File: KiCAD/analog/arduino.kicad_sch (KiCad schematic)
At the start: 50 parts, among them J11 Screw_Terminal_01x03, J12 Screw_Terminal_01x04, J13 Screw_Terminal_01x03, J14 Screw_Terminal_01x05, J16 Screw_Terminal_01x03, J17 Conn_Coaxial_Small, J18 Conn_Coaxial_Small, J19 Conn_Coaxial_Small, J20 Screw_Terminal_01x04, J21 Screw_Terminal_01x02, J22 Screw_Terminal_01x04, J23 Conn_Coaxial_Small, J24 Conn_Coaxial_Small, J6 Screw_Terminal_01x02, J7 Screw_Terminal_01x02, J8 Screw_Terminal_01x02, Q4 2N7000, Q5 2N7000, Q6 2N7000, Q7 2N7000, U1 MCP1700x-330xxTO, U17 Adafruit_PCF8575_Breakout, U18 CD14538B, U3 MCP4728

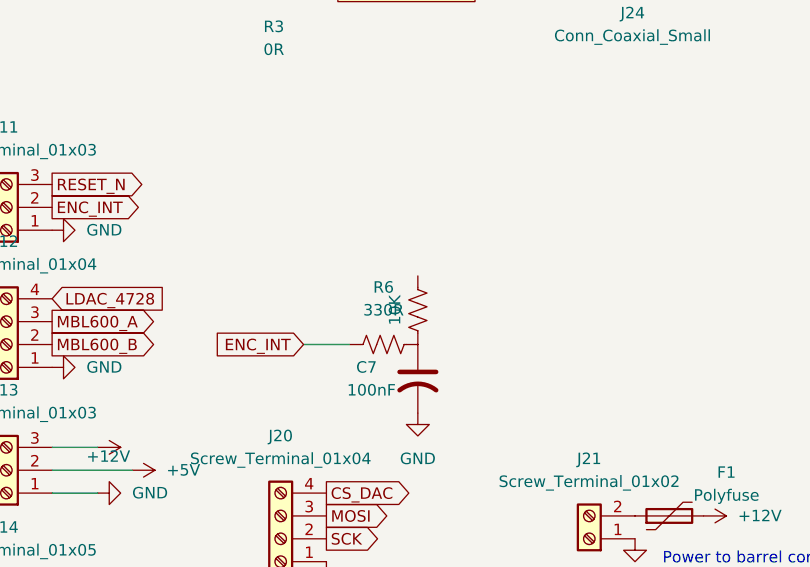
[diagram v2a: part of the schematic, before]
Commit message: KiCad revB: protoshield schematic complete + 1N4728A symbol + misc board edits
Protoshield (Metro ESP32-S3 GPIO signal conditioning):
- Full schematic drawn: series R + bypass C + Zener clamp for I_CATHODE_A/B
  (1k+100nF+1N4728A), MBL600_A/B (10k/20k divider + 22pF), GRID_BLOCK_CRASH
  (1k+100nF), ENC_INT (330R+10k pull-up), PADDLE_A/B (10k pull-ups), RESET_N
  (100nF), TR_SENSE (10k pull-up), passthrough nodes for SPI and LDAC_4728
- All THT footprints assigned (ceramic disc caps, DIN0207 resistors, Phoenix
  MKDS-1.5 2-pin/3-pin terminal blocks)
- ENC_INT wiring gap fixed (R7 re-placed to connect J4 pin 2 to ENC_INT net)
- sym-lib-table added (points to shared xmitter.kicad_sym)
- protoshield.net generated netlist added for reference

Symbol library (xmitter.kicad_sym):
- Added 1N4728A (3.3V 1W Zener, DO-41) with correct KiCad 9.0 inline pts format

Other boards:
- analog/arduino.kicad_sch: minor junction/reference adjustments after Metro
  symbol was removed to protoshield in prior session
- bias: kicad_pro and kicad_sch updated (ongoing schematic work)
- power/sym-lib-table added for new stub project

Added: Purchase Orders (JLCPCB + Digi-Key invoices), tools/_scan_symbols.py

Co-Authored-By: Claude Sonnet 4.6 <noreply@anthropic.com>
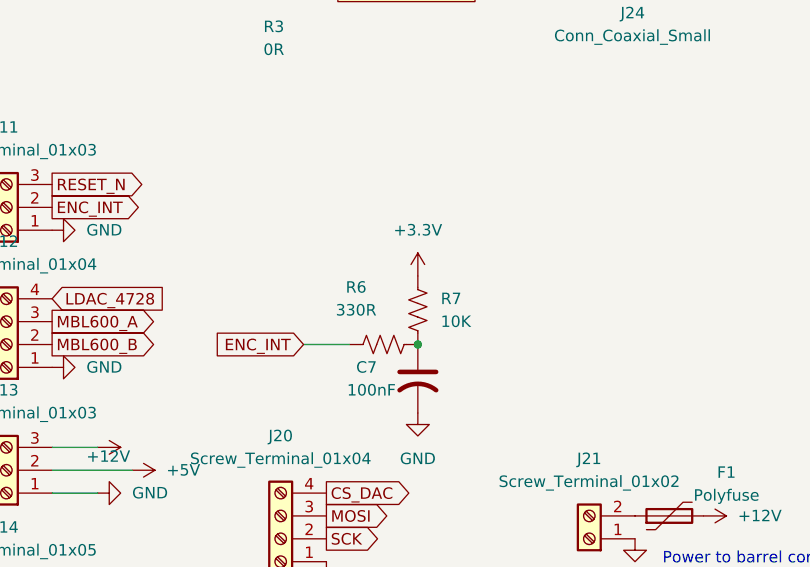
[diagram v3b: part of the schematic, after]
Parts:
- removed R102: 10K, Resistor_THT:R_Axial_DIN0207_L6.3mm_D2.5mm_P10.16mm_Horizontal, symbol Device:R_US
- added R7: 10K, symbol Device:R_US
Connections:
- net +3.3V: now also R7.1
- net at C7.1, R6.2: now also R7.2
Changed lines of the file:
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@@
 	)
 	(junction
+		(at 71.12 81.28)
+		(diameter 0)
+		(color 0 0 0 0)
+	)
+	(junction
 		(at 25.4 36.83)
 		(diameter 0)
@@
 	)
 	(symbol
+		(lib_id "power:+3.3V")
+		(at 71.12 73.66 0)
+		(unit 1)
+		(body_style 1)
+		(exclude_from_sim no)
+		(in_bom yes)
+		(on_board yes)
+		(in_pos_files yes)
+		(dnp no)
+		(fields_autoplaced yes)
+		(property "Reference" "#PWR09"
+			(at 71.12 77.47 0)
+			(hide yes)
+			(show_name no)
+			(do_not_autoplace no)
+			(effects
+				(font
+					(size 1.27 1.27)
+				)
+			)
+		)
+		(property "Value" "+3.3V"
+			(at 71.12 68.58 0)
+			(show_name no)
+			(do_not_autoplace no)
+			(effects
+				(font
+					(size 1.27 1.27)
+				)
+			)
+		)
+		(property "Footprint" ""
+			(at 71.12 73.66 0)
+			(hide yes)
+			(show_name no)
+			(do_not_autoplace no)
+			(effects
+				(font
+					(size 1.27 1.27)
+				)
+			)
+		)
+		(property "Datasheet" ""
+			(at 71.12 73.66 0)
+			(hide yes)
+			(show_name no)
+			(do_not_autoplace no)
+			(effects
+				(font
+					(size 1.27 1.27)
+				)
+			)
+		)
+		(property "Description" "Power symbol creates a global label with name \"+3.3V\""
+			(at 71.12 73.66 0)
+			(hide yes)
+			(show_name no)
+			(do_not_autoplace no)
+			(effects
+				(font
+					(size 1.27 1.27)
+				)
+			)
+		)
+		(pin "1"
+		)
+		(instances
+			(project "analog"
+				(path "/d3de40b8-856b-4fbd-829c-f45ffcd55742/2d83d0b5-86d4-4ced-ab68-6465e3dc2d72"
+					(reference "#PWR09")
+					(unit 1)
+				)
+			)
+		)
+	)
+	(symbol
 		(lib_id "Device:R_US")
 		(at 179.07 149.86 90)
@@
 	)
 	(symbol
+		(lib_id "Device:R_US")
+		(at 71.12 77.47 0)
+		(unit 1)
+		(body_style 1)
+		(exclude_from_sim no)
+		(in_bom yes)
+		(on_board yes)
+		(in_pos_files yes)
+		(dnp no)
+		(fields_autoplaced yes)
+		(property "Reference" "R7"
+			(at 73.66 76.1999 0)
+			(show_name no)
+			(do_not_autoplace no)
+			(effects
+				(font
+					(size 1.27 1.27)
+				)
+				(justify left)
+			)
+		)
+		(property "Value" "10K"
+			(at 73.66 78.7399 0)
+			(show_name no)
+			(do_not_autoplace no)
+			(effects
+				(font
+					(size 1.27 1.27)
+				)
+				(justify left)
+			)
+		)
+		(property "Footprint" ""
+			(at 72.136 77.724 90)
+			(hide yes)
+			(show_name no)
+			(do_not_autoplace no)
+			(effects
+				(font
+					(size 1.27 1.27)
+				)
+			)
+		)
+		(property "Datasheet" ""
+			(at 71.12 77.47 0)
+			(hide yes)
+			(show_name no)
+			(do_not_autoplace no)
+			(effects
+				(font
+					(size 1.27 1.27)
+				)
+			)
+		)
+		(property "Description" "Resistor, US symbol"
+			(at 71.12 77.47 0)
+			(hide yes)
+			(show_name no)
+			(do_not_autoplace no)
+			(effects
+				(font
+					(size 1.27 1.27)
+				)
+			)
+		)
+		(pin "2"
+		)
+		(pin "1"
+		)
+		(instances
+			(project "analog"
+				(path "/d3de40b8-856b-4fbd-829c-f45ffcd55742/2d83d0b5-86d4-4ced-ab68-6465e3dc2d72"
+					(reference "R7")
+					(unit 1)
+				)
+			)
+		)
+	)
+	(symbol
 		(lib_id "Connector:Conn_Coaxial_Small")
 		(at 95.25 36.83 0)
@@
 		(in_pos_files yes)
 		(dnp no)
-		(fields_autoplaced yes)
 		(property "Reference" "R6"
-			(at 67.31 74.93 90)
+			(at 64.262 74.93 90)
 			(show_name no)
 			(do_not_autoplace no)
@@
 		)
 		(property "Value" "330R"
-			(at 67.31 77.47 90)
+			(at 64.262 77.47 90)
 			(show_name no)
 			(do_not_autoplace no)
@@
 					(unit 1)
 				)
-			)
-		)
-	)
-	(symbol
-		(lib_id "Device:R_US")
-		(at 71.12 77.47 0)
-		(unit 1)
-		(body_style 1)
-		(exclude_from_sim no)
-		(in_bom yes)
-		(on_board no)
-		(in_pos_files yes)
-		(dnp no)
-		(fields_autoplaced yes)
-		(property "Reference" "R102"
-			(at 73.66 77.47 90)
-			(hide yes)
-			(show_name no)
-			(do_not_autoplace no)
-			(effects
-				(font
-					(size 1.27 1.27)
-				)
-			)
-		)
-		(property "Value" "10K"
-			(at 68.58 77.47 90)
-			(show_name no)
-			(do_not_autoplace no)
-			(effects
-				(font
-					(size 1.27 1.27)
-				)
-			)
-		)
-		(property "Footprint" "Resistor_THT:R_Axial_DIN0207_L6.3mm_D2.5mm_P10.16mm_Horizontal"
-			(at 71.12 77.47 0)
-			(hide yes)
-			(show_name no)
-			(do_not_autoplace no)
-			(effects
-				(font
-					(size 1.27 1.27)
-				)
-			)
-		)
-		(property "Datasheet" ""
-			(at 71.12 77.47 0)
-			(hide yes)
-			(show_name no)
-			(do_not_autoplace no)
-			(effects
-				(font
-					(size 1.27 1.27)
-				)
-			)
-		)
-		(property "Description" "Pull-up for future front-panel ENC_INT signal at Metro D4"
-			(at 71.12 77.47 0)
-			(hide yes)
-			(show_name no)
-			(do_not_autoplace no)
-			(effects
-				(font
-					(size 1.27 1.27)
-				)
-			)
-		)
-		(pin "1"
-		)
-		(pin "2"
-		)
-		(instances
-			(project "analog"
-				(path "/d3de40b8-856b-4fbd-829c-f45ffcd55742/2d83d0b5-86d4-4ced-ab68-6465e3dc2d72"
-					(reference "R102")
-					(unit 1)
-				)

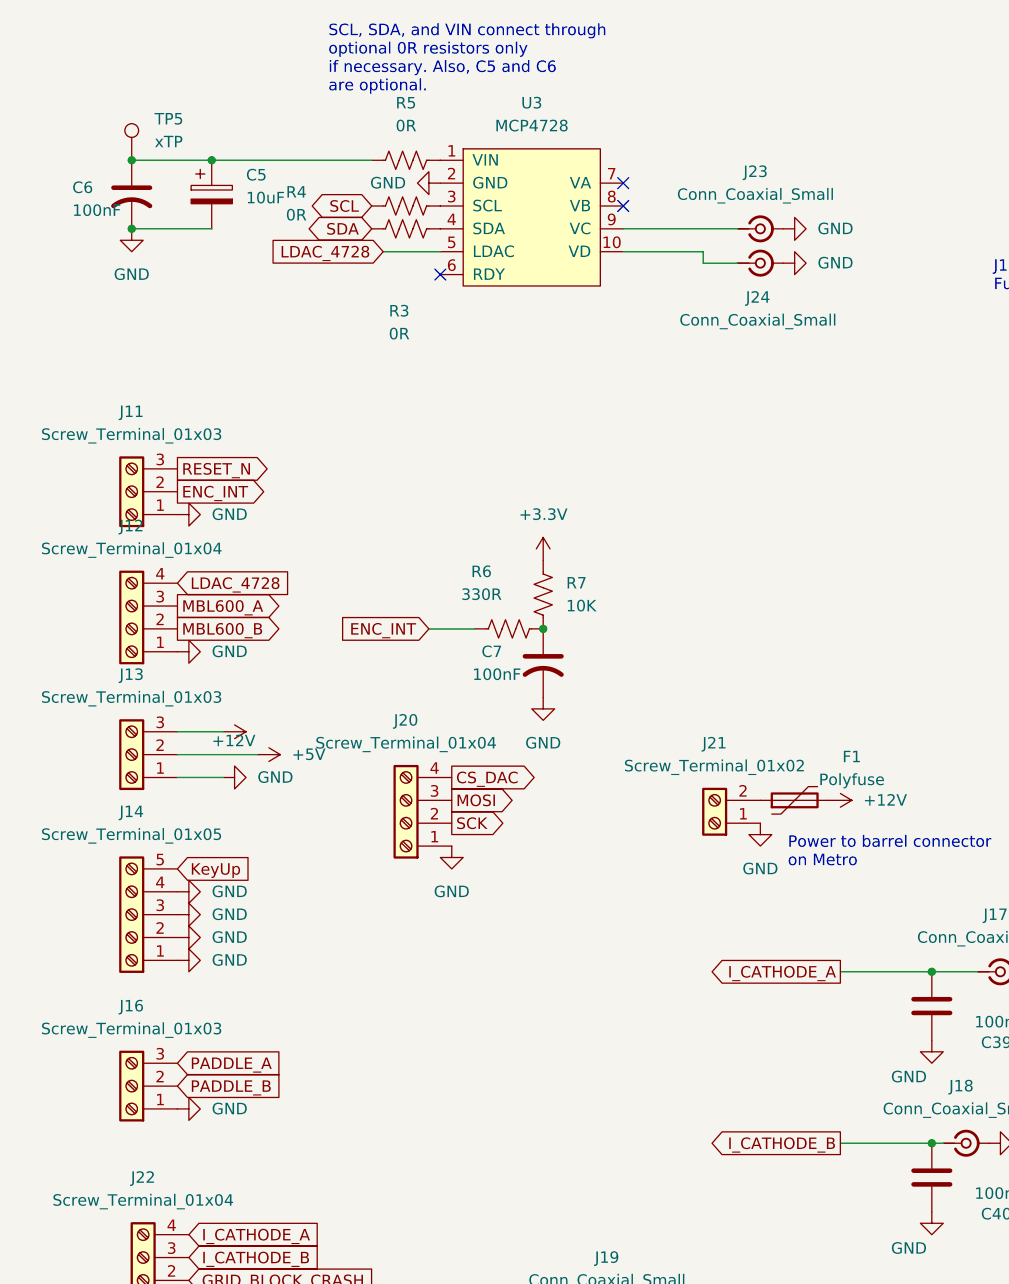
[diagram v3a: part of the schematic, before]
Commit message: KiCad revB: schematic review pass — I2C, ENC_INT, GND returns, GRID_BLOCK_CRASH clamp
Result of extended review pass against fresh netlists across all four
boards. All connectivity blockers resolved.

- Si5351 SDA/SCL wired via 0R jumpers (R8/R9) puts I2C on PCB traces
  for PCF8575 U17 and the RJ45 to the front panel. MCP4728 side has
  parallel 0R jumpers (R3/R4/R5) left DNP by default — STEMMA-QT is
  the intended path.
- ENC_INT chain unified end-to-end with staged names:
  ENC_INT_RAW (frontpanel encoder wire-OR) → ENC_INT_CLEAN (across
  CAT + analog pass-through) → ENC_INT_FINAL (post-protoshield
  conditioning). Frontpanel U4 (MCP1700-3.3 LDO) sources the +3.3V
  the pull-up R4 needs; pull-up moved to encoder side for sharper
  falling edges over the 2 m CAT run.
- Protoshield GRID_BLOCK_CRASH gets 1N4728A Zener clamp (D5),
  matching the I_CATHODE and MBL600 5V→3.3V clamp topology.
- Protoshield MBL600 conditioning rebuilt: 1K series + 100nF filter
  + 1N4728A clamp (was 10K/20K divider + 22pF that filtered nothing
  below RF).
- PADDLE_A/B and RESET_N removed from analog board — case-mounted
  switches wire directly to protoshield.
- Protoshield J1/J6 widened to 3-pin to include GND returns for the
  case-mounted paddle and reset switches.
- Bias board reference designators reorganized functionally
  (R_FA/R_FB feedback, R_GA/R_GB gain, R_PADA/R_PADB, R_GLA/R_GLB
  grid line, R_GATE, R_Z).
- New Documentation/control_board_functional_blocks.md captures
  KeyUp/Gate 2 keying, relay assignments (J6=T/R, J7=HV primary,
  J8=HV inrush), CD14538B heartbeat watchdog, TR_SENSE interlock,
  and J13 power-migration header.
- Fresh netlists exported for all four boards.

Co-Authored-By: Claude Opus 4.7 <noreply@anthropic.com>
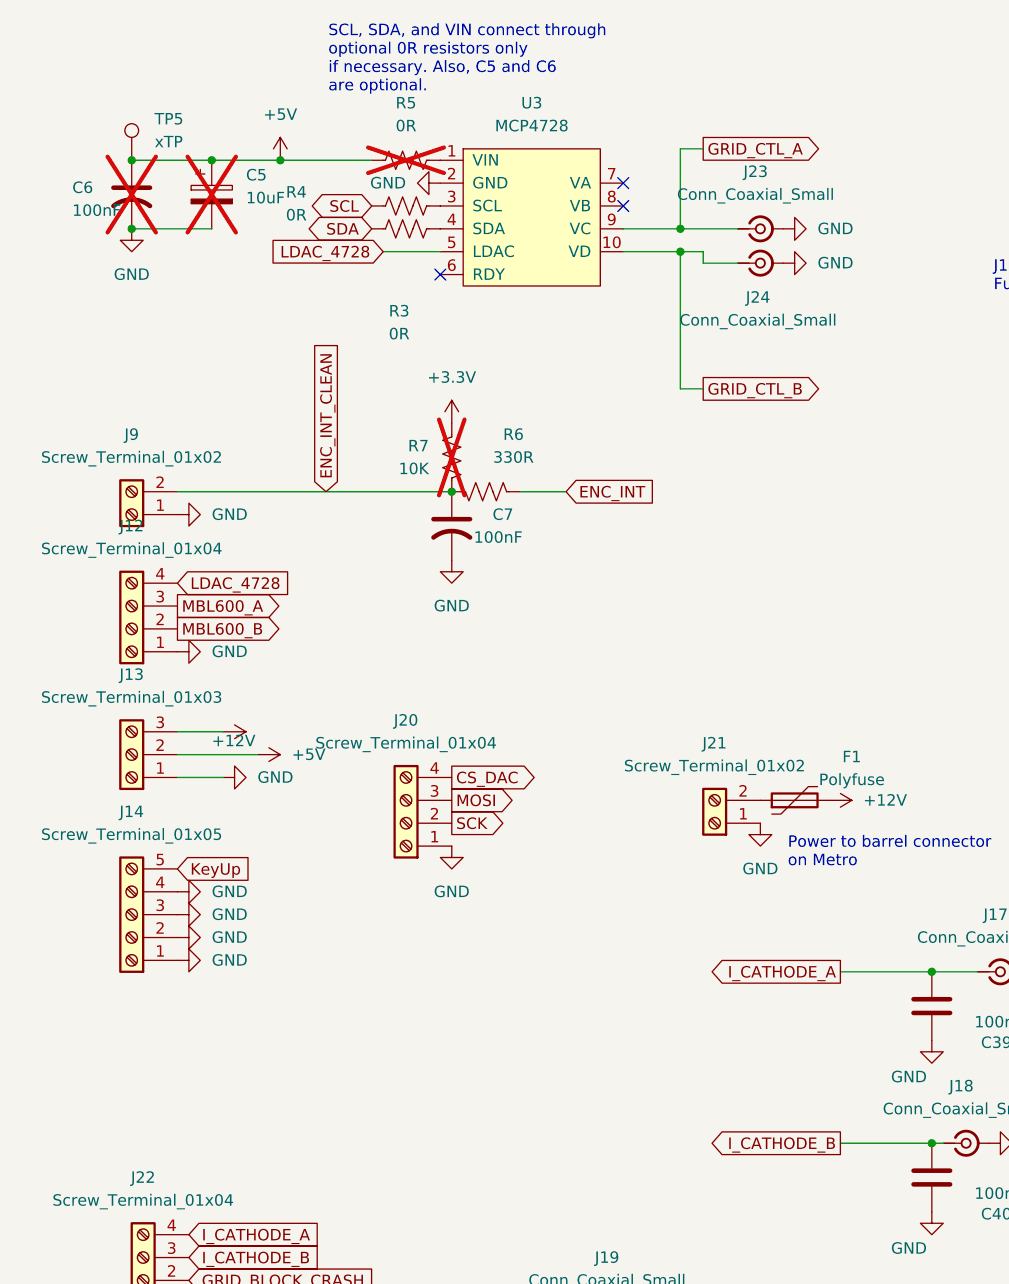
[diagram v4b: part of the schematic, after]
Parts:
- removed J11, J16: Screw_Terminal_01x03, symbol Connector:Screw_Terminal_01x03
- added J9: Screw_Terminal_01x02, symbol Connector:Screw_Terminal_01x02
- C5, C6, R5, R7: now not fitted
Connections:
- net +5V: now also C5.1, C6.1, R5.1, TP5.1
- net GND: now also J9.1 (Pin_1)
- net GRID_CTL_B: now reaches J24.1 (In), U3.10 (VD)
- net GRID_CTL_A: now reaches J23.1 (In), U3.9 (VC)
- net ENC_INT_CLEAN: now reaches C7.1, R6.2, R7.2
- net ENC_INT_CLEAN: now also J9.2 (Pin_2)
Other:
- moved on the sheet: C7, R6

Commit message: KiCad revB: assign 87 empty footprints via re-runnable scripts
Filled empty Footprint fields on capacitors, resistors, and screw
terminals across all four boards. All three scripts are re-runnable
and only fill empty fields (never overwrite existing assignments).

Scripts:
- assign_cap_footprints.py: extended CAP_LIB_IDS to also cover
  Device:C_US, Device:C_Polarized_US, Device:C_Small (was only
  Device:C and Device:C_Polarized). VALUE_TO_FOOTPRINT map unchanged.
- assign_connector_footprints.py (new): matches
  Connector:Screw_Terminal_01xNN to Phoenix MKDS-1,5-N horizontal
  P5.00mm per pin count (same pattern the protoshield already used).
- assign_resistor_footprints.py (new): matches Device:R and
  Device:R_US to the project-standard Resistor_THT:R_Axial_DIN0207
  L6.3mm_D2.5mm_P10.16mm_Horizontal footprint. All 46 populated
  resistors on the project already used this footprint; the empty
  ones now match.

Assignment counts:
- Capacitors: 42 (5 arduino, 33 vfo_complete, 2 bias, 2 frontpanel)
- Screw terminals: 17 (10 arduino, 4 bias, 1 frontpanel, 2 protoshield)
- Resistors: 28 (5 arduino, 21 vfo_complete, 2 frontpanel)

Deferred (need part-specific decisions, tracked in review notes):
- Coax connectors (12 total across analog + bias) - awaiting Cinch
  142-0701-201 footprint verification in KiCad's Connector_Coaxial
  library, or a custom footprint in xmitter.pretty/
- One-off ICs: F1 Polyfuse, U3 MCP4728, U21 LT1054
- 6 unmapped cap values in vfo_complete: 2pF x3, 220nF, 4700uF, 100uF
- U2 Metro_ESP32S3 (protoshield): intentionally empty (on_board no,
  plug-in module, not placed on PCB)

Also add three component datasheets: 1N4736AT-D (1N4728A family
reference), LM393-D, OPA1641.

Co-Authored-By: Claude Opus 4.7 <noreply@anthropic.com>
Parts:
- C3, C4: footprint (none) -> Capacitor_THT:C_Rect_L7.2mm_W4.5mm_P5.00mm
- C5: footprint (none) -> Capacitor_THT:CP_Radial_D5.0mm_P2.00mm
- C6, C7: footprint (none) -> Capacitor_THT:C_Disc_D5.0mm_W2.5mm_P5.00mm
- J12, J20, J22: footprint (none) -> TerminalBlock_Phoenix:TerminalBlock_Phoenix_MKDS-1,5-4_1x04_P5.00mm_Horizontal
- J13: footprint (none) -> TerminalBlock_Phoenix:TerminalBlock_Phoenix_MKDS-1,5-3_1x03_P5.00mm_Horizontal
- J14: footprint (none) -> TerminalBlock_Phoenix:TerminalBlock_Phoenix_MKDS-1,5-5_1x05_P5.00mm_Horizontal
- J21, J6, J7, J8, J9: footprint (none) -> TerminalBlock_Phoenix:TerminalBlock_Phoenix_MKDS-1,5-2_1x02_P5.00mm_Horizontal
- R3, R4, R5, R6, R7: footprint (none) -> Resistor_THT:R_Axial_DIN0207_L6.3mm_D2.5mm_P10.16mm_Horizontal
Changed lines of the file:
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@@
 			)
 		)
-		(property "Footprint" ""
+		(property "Footprint" "Capacitor_THT:C_Disc_D5.0mm_W2.5mm_P5.00mm"
 			(at 25.4 33.02 0)
 			(hide yes)
@@
 			)
 		)
-		(property "Footprint" ""
+		(property "Footprint" "Resistor_THT:R_Axial_DIN0207_L6.3mm_D2.5mm_P10.16mm_Horizontal"
 			(at 59.944 62.484 90)
 			(hide yes)
@@
 			)
 		)
-		(property "Footprint" ""
+		(property "Footprint" "TerminalBlock_Phoenix:TerminalBlock_Phoenix_MKDS-1,5-2_1x02_P5.00mm_Horizontal"
 			(at 219.71 59.69 0)
 			(hide yes)
@@
 			)
 		)
-		(property "Footprint" ""
+		(property "Footprint" "Resistor_THT:R_Axial_DIN0207_L6.3mm_D2.5mm_P10.16mm_Horizontal"
 			(at 64.516 65.024 90)
 			(hide yes)
@@
 			)
 		)
-		(property "Footprint" ""
+		(property "Footprint" "TerminalBlock_Phoenix:TerminalBlock_Phoenix_MKDS-1,5-2_1x02_P5.00mm_Horizontal"
 			(at 90.17 102.87 0)
 			(hide yes)
@@
 			)
 		)
-		(property "Footprint" ""
+		(property "Footprint" "TerminalBlock_Phoenix:TerminalBlock_Phoenix_MKDS-1,5-4_1x04_P5.00mm_Horizontal"
 			(at 25.4 81.28 0)
 			(hide yes)
@@
 			)
 		)
-		(property "Footprint" ""
+		(property "Footprint" "TerminalBlock_Phoenix:TerminalBlock_Phoenix_MKDS-1,5-2_1x02_P5.00mm_Horizontal"
 			(at 25.4 68.58 0)
 			(hide yes)
@@
 			)
 		)
-		(property "Footprint" ""
+		(property "Footprint" "TerminalBlock_Phoenix:TerminalBlock_Phoenix_MKDS-1,5-2_1x02_P5.00mm_Horizontal"
 			(at 248.92 88.9 0)
 			(hide yes)
@@
 			)
 		)
-		(property "Footprint" ""
+		(property "Footprint" "Resistor_THT:R_Axial_DIN0207_L6.3mm_D2.5mm_P10.16mm_Horizontal"
 			(at 56.134 33.274 90)
 			(hide yes)
@@
 			)
 		)
-		(property "Footprint" ""
+		(property "Footprint" "Resistor_THT:R_Axial_DIN0207_L6.3mm_D2.5mm_P10.16mm_Horizontal"
 			(at 56.134 35.814 90)
 			(hide yes)
@@
 			)
 		)
-		(property "Footprint" ""
+		(property "Footprint" "TerminalBlock_Phoenix:TerminalBlock_Phoenix_MKDS-1,5-5_1x05_P5.00mm_Horizontal"
 			(at 25.4 113.03 0)
 			(hide yes)
@@
 			)
 		)
-		(property "Footprint" ""
+		(property "Footprint" "TerminalBlock_Phoenix:TerminalBlock_Phoenix_MKDS-1,5-4_1x04_P5.00mm_Horizontal"
 			(at 26.67 153.67 0)
 			(hide yes)
@@
 			)
 		)
-		(property "Footprint" ""
+		(property "Footprint" "Resistor_THT:R_Axial_DIN0207_L6.3mm_D2.5mm_P10.16mm_Horizontal"
 			(at 56.134 28.194 90)
 			(hide yes)
@@
 			)
 		)
-		(property "Footprint" ""
+		(property "Footprint" "TerminalBlock_Phoenix:TerminalBlock_Phoenix_MKDS-1,5-4_1x04_P5.00mm_Horizontal"
 			(at 55.88 102.87 0)
 			(hide yes)
@@
 			)
 		)
-		(property "Footprint" ""
+		(property "Footprint" "TerminalBlock_Phoenix:TerminalBlock_Phoenix_MKDS-1,5-2_1x02_P5.00mm_Horizontal"
 			(at 219.71 109.22 0)
 			(hide yes)
@@
 			)
 		)
-		(property "Footprint" ""
+		(property "Footprint" "Capacitor_THT:C_Rect_L7.2mm_W4.5mm_P5.00mm"
 			(at 165.1 34.29 0)
 			(hide yes)
@@
 			)
 		)
-		(property "Footprint" ""
+		(property "Footprint" "Capacitor_THT:C_Rect_L7.2mm_W4.5mm_P5.00mm"
 			(at 184.15 34.29 0)
 			(hide yes)
@@
 			)
 		)
-		(property "Footprint" ""
+		(property "Footprint" "Capacitor_THT:CP_Radial_D5.0mm_P2.00mm"
 			(at 35.2552 36.83 0)
 			(hide yes)
@@
 			)
 		)
-		(property "Footprint" ""
+		(property "Footprint" "TerminalBlock_Phoenix:TerminalBlock_Phoenix_MKDS-1,5-3_1x03_P5.00mm_Horizontal"
 			(at 25.4 95.25 0)
 			(hide yes)
@@
 			)
 		)
-		(property "Footprint" ""
+		(property "Footprint" "Capacitor_THT:C_Disc_D5.0mm_W2.5mm_P5.00mm"
 			(at 60.96 69.85 0)
 			(hide yes)
